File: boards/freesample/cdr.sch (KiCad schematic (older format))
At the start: 6 parts

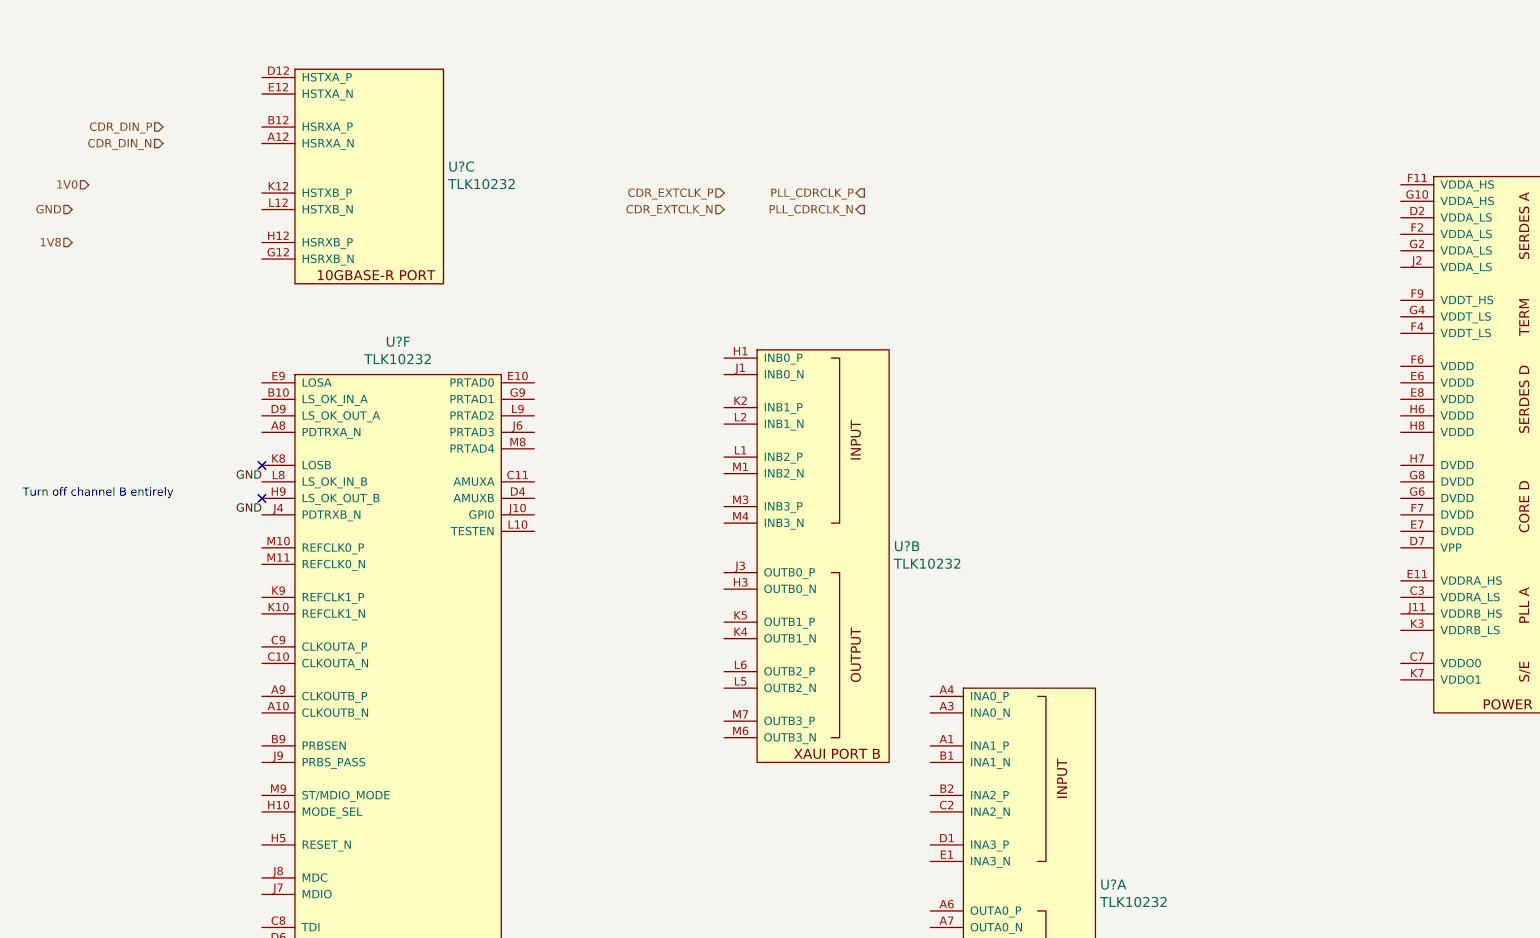
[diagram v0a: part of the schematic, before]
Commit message: Continued initial schematic capture
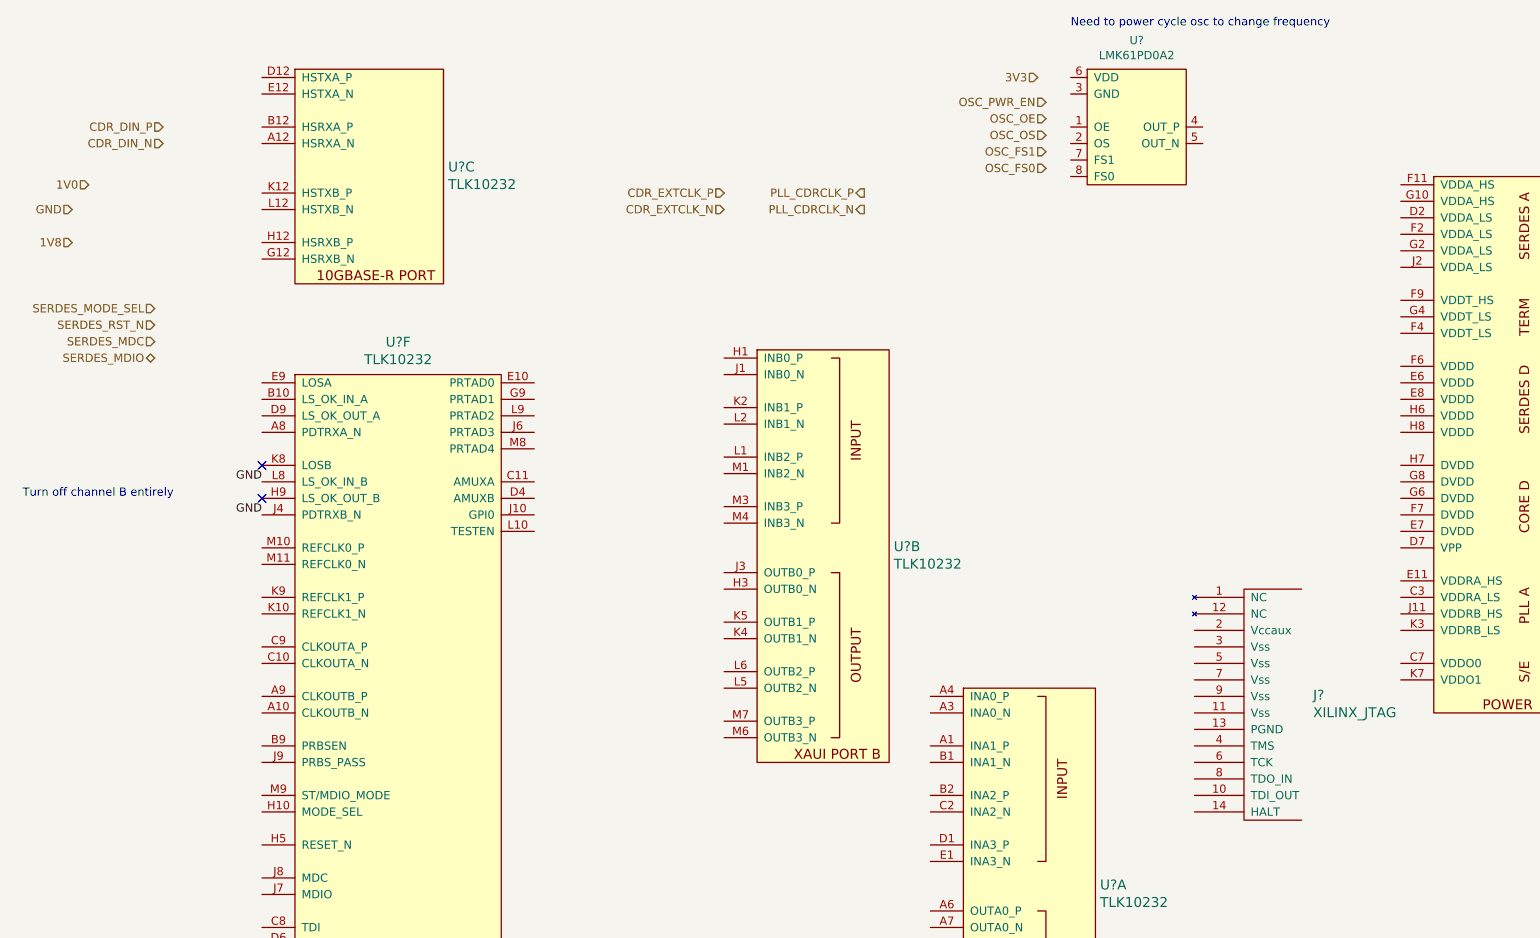
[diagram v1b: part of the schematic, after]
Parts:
- added J?: XILINX_JTAG, symbol xilinx-azonenberg:XILINX_JTAG
- added U?: LMK61PD0A2, symbol special-azonenberg:LMK61PD0A2
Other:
- note added: "Need to power cycle osc to change frequency"
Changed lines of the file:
@@
 $Descr A4 11693 8268
 encoding utf-8
-Sheet 4 11
+Sheet 4 12
 Title "FREESAMPLE Oscilloscope"
-Date "2018-12-15"
+Date "2018-12-17"
 Rev "0.1"
 Comp "Andrew D. Zonenberg / Antikernel Labs"
@@
 Text HLabel 900  1850 0    50   Input ~ 0
 1V8
+Text HLabel 1400 2250 0    50   Input ~ 0
+SERDES_MODE_SEL
+Text HLabel 1400 2350 0    50   Input ~ 0
+SERDES_RST_N
+Text HLabel 1400 2450 0    50   Input ~ 0
+SERDES_MDC
+Text HLabel 1400 2550 0    50   BiDi ~ 0
+SERDES_MDIO
+$Comp
+L xilinx-azonenberg:XILINX_JTAG J?
+U 1 1 5C2B9BAA
+P 7700 5300
+F 0 "J?" H 8419 6008 60  0000 L CNN
+F 1 "XILINX_JTAG" H 8419 5902 60  0000 L CNN
+F 2 "" H 7700 5300 60  0000 C CNN
+F 3 "" H 7700 5300 60  0000 C CNN
+	1    7700 5300
+	1    0    0    -1
+$EndComp
+$Comp
+L special-azonenberg:LMK61PD0A2 U?
+U 1 1 5C335B5F
+P 7050 1500
+AR Path="/5C158069/5C335B5F" Ref="U?"  Part="1"
+AR Path="/5C15803C/5C335B5F" Ref="U?"  Part="1"
+F 0 "U?" H 7350 2375 50  0000 C CNN
+F 1 "LMK61PD0A2" H 7350 2284 50  0000 C CNN
+F 2 "" H 7300 1450 50  0001 C CNN
+F 3 "" H 7300 1450 50  0001 C CNN
+	1    7050 1500
+	1    0    0    -1
+$EndComp
+Text HLabel 6800 1000 0    50   Input ~ 0
+OSC_PWR_EN
+Text Notes 6950 550  0    50   ~ 0
+Need to power cycle osc to change frequency
+Text HLabel 6800 1100 0    50   Input ~ 0
+OSC_OE
+Text HLabel 6800 1200 0    50   Input ~ 0
+OSC_OS
+Text HLabel 6800 1300 0    50   Input ~ 0
+OSC_FS1
+Text HLabel 6800 1400 0    50   Input ~ 0
+OSC_FS0
+Text HLabel 6750 850  0    50   Input ~ 0
+3V3
 $EndSCHEMATC

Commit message: Continued work on schematic capture
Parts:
- added C100, C101, C102, C58, C60, C75, C79, C80, C81, C82, C83, C84, C85, C86, C87, C88, C89, C90, C91, C92, C93, C94, C95, C96, C97, C98, C99: 0.47 uF, symbol device:C
- added C56, C57, C61, C62, C63, C64, C65, C66: 0.1 uF, symbol device:C
- added C59, C67, C68, C69, C70, C71, C72, C73, C74, C76, C77, C78: 4.7 uF, symbol device:C
- added FB2, FB3, FB4: TBD, symbol passive-azonenberg:INDUCTOR_PWROUT
- added R10, R2, R3, R4, R5, R6, R7, R8, R9: 100, symbol device:R
- added R11: 1K, symbol device:R
- added R12: 33, symbol device:R
- added R13: 10K, symbol device:R
- added U13: SIP32408, symbol power-azonenberg:SIP32408
- gave numbers to parts that had none: 3
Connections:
- net 1V0: now also U5.D7 (VPP), U5.E6 (VDDD), U5.E7 (DVDD), U5.E8 (VDDD), U5.F6 (VDDD), U5.F7 (DVDD), U5.G6 (DVDD), U5.G8 (DVDD), U5.H6 (VDDD), U5.H7 (DVDD), U5.H8 (VDDD), C101.1, C102.1, C67.1, C68.1, C69.1, C70.1, C73.1, C74.1, C79.1, C80.1, C86.1, C87.1, C92.1, C93.1, C98.1, C99.1, FB2.2, FB3.2
- net 1V8: now also J6.2 (Vccaux), U5.B10 (LS_OK_IN_A), U5.C7 (VDDO0), U5.K7 (VDDO1), C71.1, C72.1, C75.1, C81.1, FB4.2, R11.2, R13.2
- net 3V3: now also C58.1, U13.1 (IN)
- net CDR_DIN_N: now also C57.2
- net CDR_DIN_P: now also C56.2
- net CDR_EXTCLK_N: now also C64.2
- net CDR_EXTCLK_P: now also C63.2
- net GND: now also J6.11 (Vss), J6.3 (Vss), J6.5 (Vss), J6.7 (Vss), J6.9 (Vss), U5.A11 (GND), U5.A2 (GND), U5.A5 (GND), U5.B11 (GND), U5.B3 (GND), U5.B4 (GND), U5.B7 (GND), U5.B9 (PRBSEN), U5.C1 (GND), U5.C12 (GND), U5.C6 (GND), U5.D10 (GND), U5.D11 (GND), U5.D3 (GND), U5.D5 (GND), U5.E2 (GND), U5.E4 (GND), U5.F1 (GND), U5.F10 (GND), U5.F12 (GND), U5.F5 (GND), U5.F8 (GND), U5.G1 (GND), U5.G11 (GND), U5.G3 (GND), U5.G5 (GND), U5.G7 (GND), U5.H11 (GND), U5.H2 (GND), U5.H4 (GND), U5.J12 (GND), U5.J5 (GND), U5.K1 (GND), U5.K11 (GND), U5.K6 (GND), U5.L11 (GND), U5.L3 (GND), U5.L4 (GND), U5.L7 (GND), U5.M12 (GND), U5.M2 (GND), U5.M5 (GND), U6.3 (GND), C100.2, C101.2, C102.2, C58.2, C59.2, C60.2, C67.2, C68.2, C69.2, C70.2, C71.2, C72.2, C73.2, C74.2, C75.2, C76.2, C77.2, C78.2, C79.2, C80.2, C81.2, C82.2, C83.2, C84.2, C85.2, C86.2, C87.2, C88.2, C89.2, C90.2, C91.2, C92.2, C93.2, C94.2, C95.2, C96.2, C97.2, C98.2, C99.2, R10.2, R2.2, R3.2, R4.2, R5.2, R6.2, R7.2, R8.2, R9.2, U13.2 (GND), U13.PAD (GND)
- net OSC_FS0: now also U6.8 (FS0)
- net OSC_FS1: now also U6.7 (FS1)
- net OSC_OE: now also U6.1 (OE)
- net OSC_OS: now also U6.2 (OS)
- net OSC_PWR_EN: now also U13.3 (EN)
- net PLL_CDRCLK_N: now also C66.2
- net PLL_CDRCLK_P: now also C65.2
- net SERDES_MDC: now also U5.J8 (MDC)
- net SERDES_MDIO: now also U5.J7 (MDIO)
- net SERDES_MODE_SEL: now also U5.H10 (MODE_SEL)
- net SERDES_RST_N: now also U5.H5 (RESET_N)
- net at U5.A1 (INA1_P): now also U5.B1 (INA1_N), R8.1
- net at U5.A3 (INA0_N): now also U5.A4 (INA0_P), R7.1
- net at U5.B2 (INA2_P): now also U5.C2 (INA2_N), R9.1
- net at U5.D1 (INA3_P): now also U5.E1 (INA3_N), R10.1
- net at U5.H1 (INB0_P): now also U5.J1 (INB0_N), R3.1
- net at U5.K2 (INB1_P): now also U5.L2 (INB1_N), R4.1
- net at U5.L1 (INB2_P): now also U5.M1 (INB2_N), R5.1
- net at U5.M3 (INB3_P): now also U5.M4 (INB3_N), R6.1
- net CDR_DIN_AC_N: now reaches U5.A12 (HSRXA_N)
- net CDR_DIN_AC_N: now also C57.1
- net CDR_DIN_AC_P: now reaches U5.B12 (HSRXA_P)
- net CDR_DIN_AC_P: now also C56.1
- net at U5.G12 (HSRXB_N): now also U5.H12 (HSRXB_P), R2.1
- net A1V8_PLL_SERDES: now reaches U5.C3 (VDDRA_LS)
- net A1V8_PLL_SERDES: now also U5.E11 (VDDRA_HS), U5.J11 (VDDRB_HS), U5.K3 (VDDRB_LS), C100.1, C78.1, C85.1, C91.1, C97.1, FB4.1
- net A1V0_SERDES: now reaches U5.D2 (VDDA_LS)
- net A1V0_SERDES: now also U5.F11 (VDDA_HS), U5.F2 (VDDA_LS), U5.G10 (VDDA_HS), U5.G2 (VDDA_LS), U5.J2 (VDDA_LS), C76.1, C82.1, C83.1, C88.1, C89.1, C94.1, C95.1, FB2.1
- net A1V0T_SERDES: now reaches U5.F4 (VDDT_LS)
- net A1V0T_SERDES: now also U5.F9 (VDDT_HS), U5.G4 (VDDT_LS), C77.1, C84.1, C90.1, C96.1, FB3.1
- net SERDES_TMS: now reaches U5.B8 (TMS)
- net SERDES_TMS: now also J6.4 (TMS)
- net SCLKO_DC_N: now reaches U5.C10 (CLKOUTA_N)
- net SCLKO_DC_N: now also C66.1
- net SERDES_TDI: now reaches U5.C8 (TDI)
- net SERDES_TDI: now also J6.10 (TDI_OUT)
- net SCLKO_DC_P: now reaches U5.C9 (CLKOUTA_P)
- net SCLKO_DC_P: now also C65.1
- net at U5.D6 (TDO): now also R12.1
- net SERDES_TCK: now reaches U5.D8 (TCK)
- net SERDES_TCK: now also J6.6 (TCK)
- net at U5.E5 (TRST_N): now also R13.1
- net SRC1_AC_N: now reaches U5.K10 (REFCLK1_N)
- net SRC1_AC_N: now also C64.1
- net SRC1_AC_P: now reaches U5.K9 (REFCLK1_P)
- net SRC1_AC_P: now also C63.1
- net SRC0_AC_P: now reaches U5.M10 (REFCLK0_P)
- net SRC0_AC_P: now also C61.1
- net SRC0_AC_N: now reaches U5.M11 (REFCLK0_N)
- net SRC0_AC_N: now also C62.1
- net at U5.M9 (ST/MDIO_MODE): now also R11.1
- net SERDES_TDO: now reaches J6.8 (TDO_IN)
- net SERDES_TDO: now also R12.2
- net SERDES_REFCLK0_P: now reaches U6.4 (OUT_P)
- net SERDES_REFCLK0_P: now also C61.2
- net SERDES_REFCLK0_N: now reaches U6.5 (OUT_N)
- net SERDES_REFCLK0_N: now also C62.2
- net OSC_VDD: now reaches U6.6 (VDD)
- net OSC_VDD: now also C59.1, C60.1, U13.4 (OUT)
- no-connect marks 2 -> 29
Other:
- note added: "Channel B not used"
- note added: "Digital SERDES decoupling"
- note added: "Digital core decoupling"
- note added: "Max 15 MHz JTAG"
- note added: "PLL decoupling"
- note added: "SERDES analog decoupling"
- note added: "Termination decoupling"
- note added: "VDDO decoupling"
- note removed: "Turn off channel B entirely"
- moved on the sheet: J6, U5A, U5B, U5D, U5E, U5F, U6

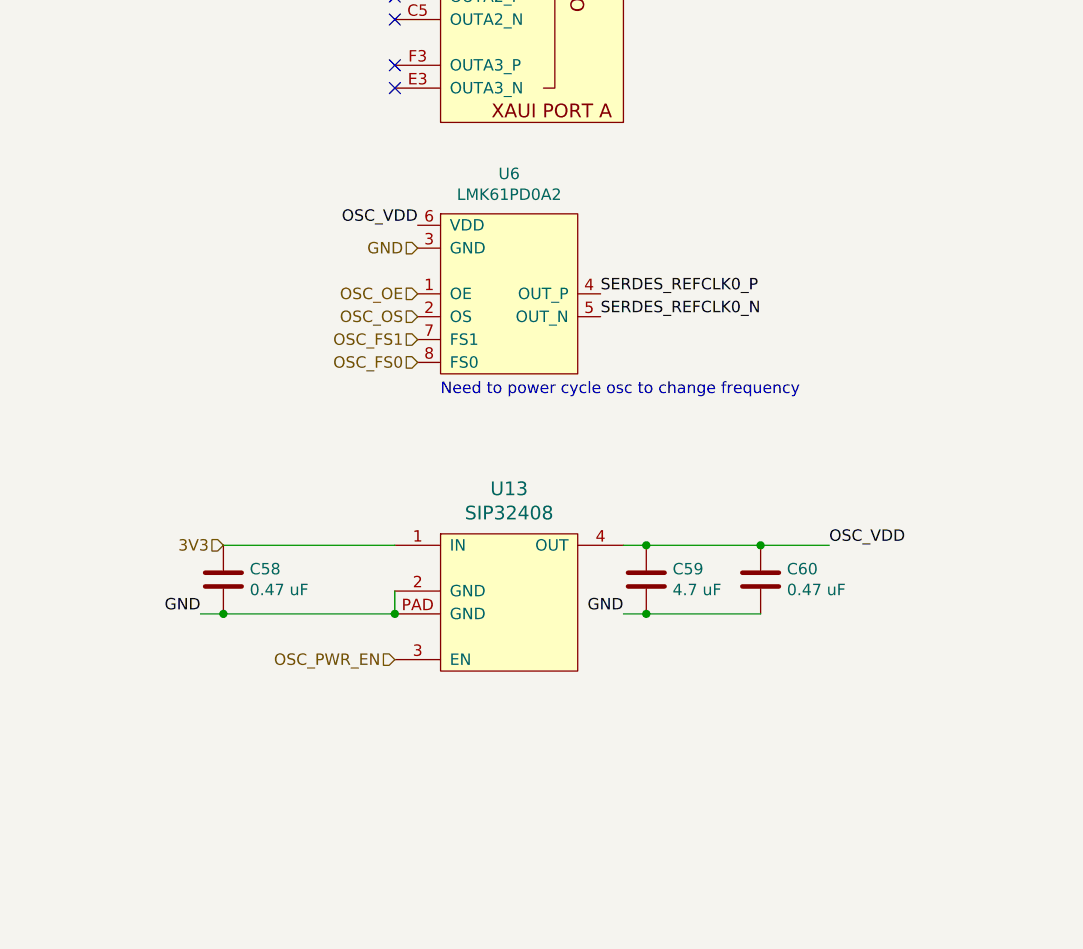
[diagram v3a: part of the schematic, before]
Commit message: Lots more work on PSU and sch readability improvements
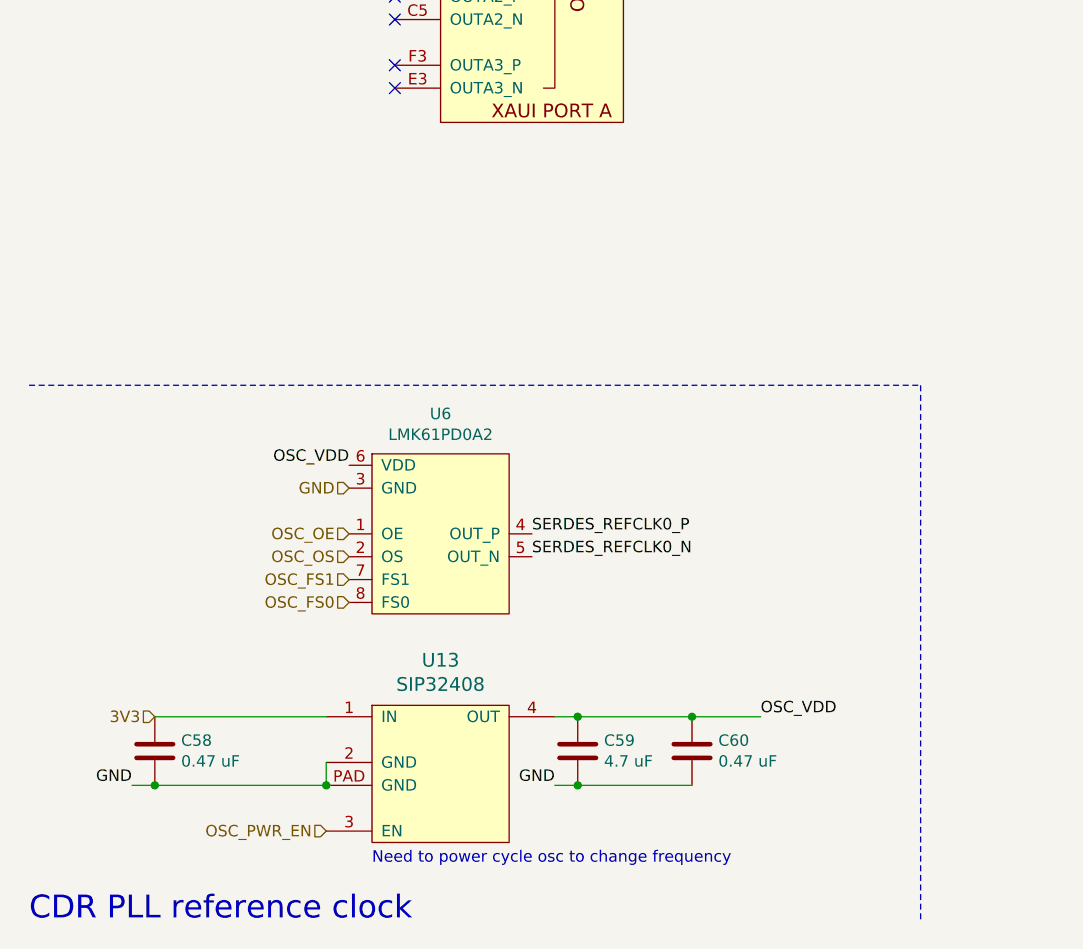
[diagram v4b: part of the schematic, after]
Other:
- note added: "CDR PLL reference clock"
- moved on the sheet: C58, C59, C60, U13, U6
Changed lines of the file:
@@
 Text HLabel 13300 1800 0    50   Input ~ 0
 1V0
-Text HLabel 2250 8200 0    50   Input ~ 0
+Text HLabel 1950 9250 0    50   Input ~ 0
 GND
 Text HLabel 13300 3600 0    50   Input ~ 0
@@
 L special-azonenberg:LMK61PD0A2 U?
 U 1 1 5C335B5F
-P 2350 8750
+P 2050 9800
 AR Path="/5C158069/5C335B5F" Ref="U?"  Part="1"
 AR Path="/5C15803C/5C335B5F" Ref="U6"  Part="1"
-F 0 "U6" H 2650 9625 50  0000 C CNN
-F 1 "LMK61PD0A2" H 2650 9534 50  0000 C CNN
-F 2 "" H 2600 8700 50  0001 C CNN
-F 3 "" H 2600 8700 50  0001 C CNN
-	1    2350 8750
-	1    0    0    -1
-$EndComp
-Text HLabel 2150 10000 0    50   Input ~ 0
+F 0 "U6" H 2350 10675 50  0000 C CNN
+F 1 "LMK61PD0A2" H 2350 10584 50  0000 C CNN
+F 2 "" H 2300 9750 50  0001 C CNN
+F 3 "" H 2300 9750 50  0001 C CNN
+	1    2050 9800
+	1    0    0    -1
+$EndComp
+Text HLabel 1850 10750 0    50   Input ~ 0
 OSC_PWR_EN
-Text Notes 2350 8850 0    50   ~ 0
+Text Notes 2050 10900 0    50   ~ 0
 Need to power cycle osc to change frequency
-Text HLabel 2250 8400 0    50   Input ~ 0
+Text HLabel 1950 9450 0    50   Input ~ 0
 OSC_OE
-Text HLabel 2250 8500 0    50   Input ~ 0
+Text HLabel 1950 9550 0    50   Input ~ 0
 OSC_OS
-Text HLabel 2250 8600 0    50   Input ~ 0
+Text HLabel 1950 9650 0    50   Input ~ 0
 OSC_FS1
-Text HLabel 2250 8700 0    50   Input ~ 0
+Text HLabel 1950 9750 0    50   Input ~ 0
 OSC_FS0
-Text HLabel 1400 9500 0    50   Input ~ 0
+Text HLabel 1100 10250 0    50   Input ~ 0
 3V3
 $Comp
@@
 SERDES_TDI
 NoConn ~ 5200 6100
-Text Label 2250 8100 2    50   ~ 0
+Text Label 1950 9150 2    50   ~ 0
 OSC_VDD
-Text Label 3050 8400 0    50   ~ 0
+Text Label 2750 9450 0    50   ~ 0
 SERDES_REFCLK0_P
-Text Label 3050 8500 0    50   ~ 0
+Text Label 2750 9550 0    50   ~ 0
 SERDES_REFCLK0_N
 Text Label 14650 600  2    50   ~ 0
@@
 L device:C C59
 U 1 1 5C86CE31
-P 3250 9650
-F 0 "C59" H 3365 9696 50  0000 L CNN
-F 1 "4.7 uF" H 3365 9605 50  0000 L CNN
-F 2 "" H 3288 9500 50  0001 C CNN
-F 3 "" H 3250 9650 50  0001 C CNN
-	1    3250 9650
+P 2950 10400
+F 0 "C59" H 3065 10446 50  0000 L CNN
+F 1 "4.7 uF" H 3065 10355 50  0000 L CNN
+F 2 "" H 2988 10250 50  0001 C CNN
+F 3 "" H 2950 10400 50  0001 C CNN
+	1    2950 10400
 	1    0    0    -1
 $EndComp
@@
 L device:C C60
 U 1 1 5C86D093
-P 3750 9650
-F 0 "C60" H 3865 9696 50  0000 L CNN
-F 1 "0.47 uF" H 3865 9605 50  0000 L CNN
-F 2 "" H 3788 9500 50  0001 C CNN
-F 3 "" H 3750 9650 50  0001 C CNN
-	1    3750 9650
+P 3450 10400
+F 0 "C60" H 3565 10446 50  0000 L CNN
+F 1 "0.47 uF" H 3565 10355 50  0000 L CNN
+F 2 "" H 3488 10250 50  0001 C CNN
+F 3 "" H 3450 10400 50  0001 C CNN
+	1    3450 10400
 	1    0    0    -1
 $EndComp
@@
 L power-azonenberg:SIP32408 U13
 U 1 1 5C878F99
-P 2350 10050
-F 0 "U13" H 2650 10847 60  0000 C CNN
-F 1 "SIP32408" H 2650 10741 60  0000 C CNN
-F 2 "" H 2350 10050 60  0000 C CNN
-F 3 "" H 2350 10050 60  0000 C CNN
-	1    2350 10050
-	1    0    0    -1
-$EndComp
-Text Label 1300 9800 2    50   ~ 0
+P 2050 10800
+F 0 "U13" H 2350 11597 60  0000 C CNN
+F 1 "SIP32408" H 2350 11491 60  0000 C CNN
+F 2 "" H 2050 10800 60  0000 C CNN
+F 3 "" H 2050 10800 60  0000 C CNN
+	1    2050 10800
+	1    0    0    -1
+$EndComp
+Text Label 1000 10550 2    50   ~ 0
 GND
 Wire Wire Line
-	2150 9700 2150 9800
-Text Label 4050 9500 0    50   ~ 0
+	1850 10450 1850 10550
+Text Label 3750 10250 0    50   ~ 0
 OSC_VDD
 Wire Wire Line
-	4050 9500 3750 9500
-Connection ~ 3250 9500
-Wire Wire Line
-	3250 9500 3150 9500
-Connection ~ 3750 9500
-Wire Wire Line
-	3750 9500 3250 9500
-Text Label 3150 9800 2    50   ~ 0
+	3750 10250 3450 10250
+Connection ~ 2950 10250
+Wire Wire Line
+	2950 10250 2850 10250
+Connection ~ 3450 10250
+Wire Wire Line
+	3450 10250 2950 10250
+Text Label 2850 10550 2    50   ~ 0
 GND
 Wire Wire Line
-	3150 9800 3250 9800
-Connection ~ 3250 9800
-Wire Wire Line
-	3250 9800 3750 9800
+	2850 10550 2950 10550
+Connection ~ 2950 10550
+Wire Wire Line
+	2950 10550 3450 10550
 $Comp
 L device:C C58
 U 1 1 5C8A7B27
-P 1400 9650
-F 0 "C58" H 1515 9696 50  0000 L CNN
-F 1 "0.47 uF" H 1515 9605 50  0000 L CNN
-F 2 "" H 1438 9500 50  0001 C CNN
-F 3 "" H 1400 9650 50  0001 C CNN
-	1    1400 9650
-	1    0    0    -1
-$EndComp
-Wire Wire Line
-	1400 9500 2150 9500
-Wire Wire Line
-	2150 9800 1400 9800
-Connection ~ 2150 9800
-Wire Wire Line
-	1300 9800 1400 9800
-Connection ~ 1400 9800
+P 1100 10400
+F 0 "C58" H 1215 10446 50  0000 L CNN
+F 1 "0.47 uF" H 1215 10355 50  0000 L CNN
+F 2 "" H 1138 10250 50  0001 C CNN
+F 3 "" H 1100 10400 50  0001 C CNN
+	1    1100 10400
+	1    0    0    -1
+$EndComp
+Wire Wire Line
+	1100 10250 1850 10250
+Wire Wire Line
+	1850 10550 1100 10550
+Connection ~ 1850 10550
+Wire Wire Line
+	1000 10550 1100 10550
+Connection ~ 1100 10550
+Wire Notes Line width 20 style solid
+	550  8800 4450 8800
+Wire Notes Line width 20 style solid
+	4450 8800 4450 11150
+Text Notes 550  11150 0    100  ~ 0
+CDR PLL reference clock
 $EndSCHEMATC
